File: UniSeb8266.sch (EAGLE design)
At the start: 31 parts, among them IC1 WEMOS-D1-MINI, IC2 GY-BME280-3.3, IC3 LM3940, IC4 MCP23008SS, IC5 RT9400, IC6 AMS5915, J1 22-27-2031-03, X61 JST-XH-05-PIN-LONG-PAD, X7 0446200002

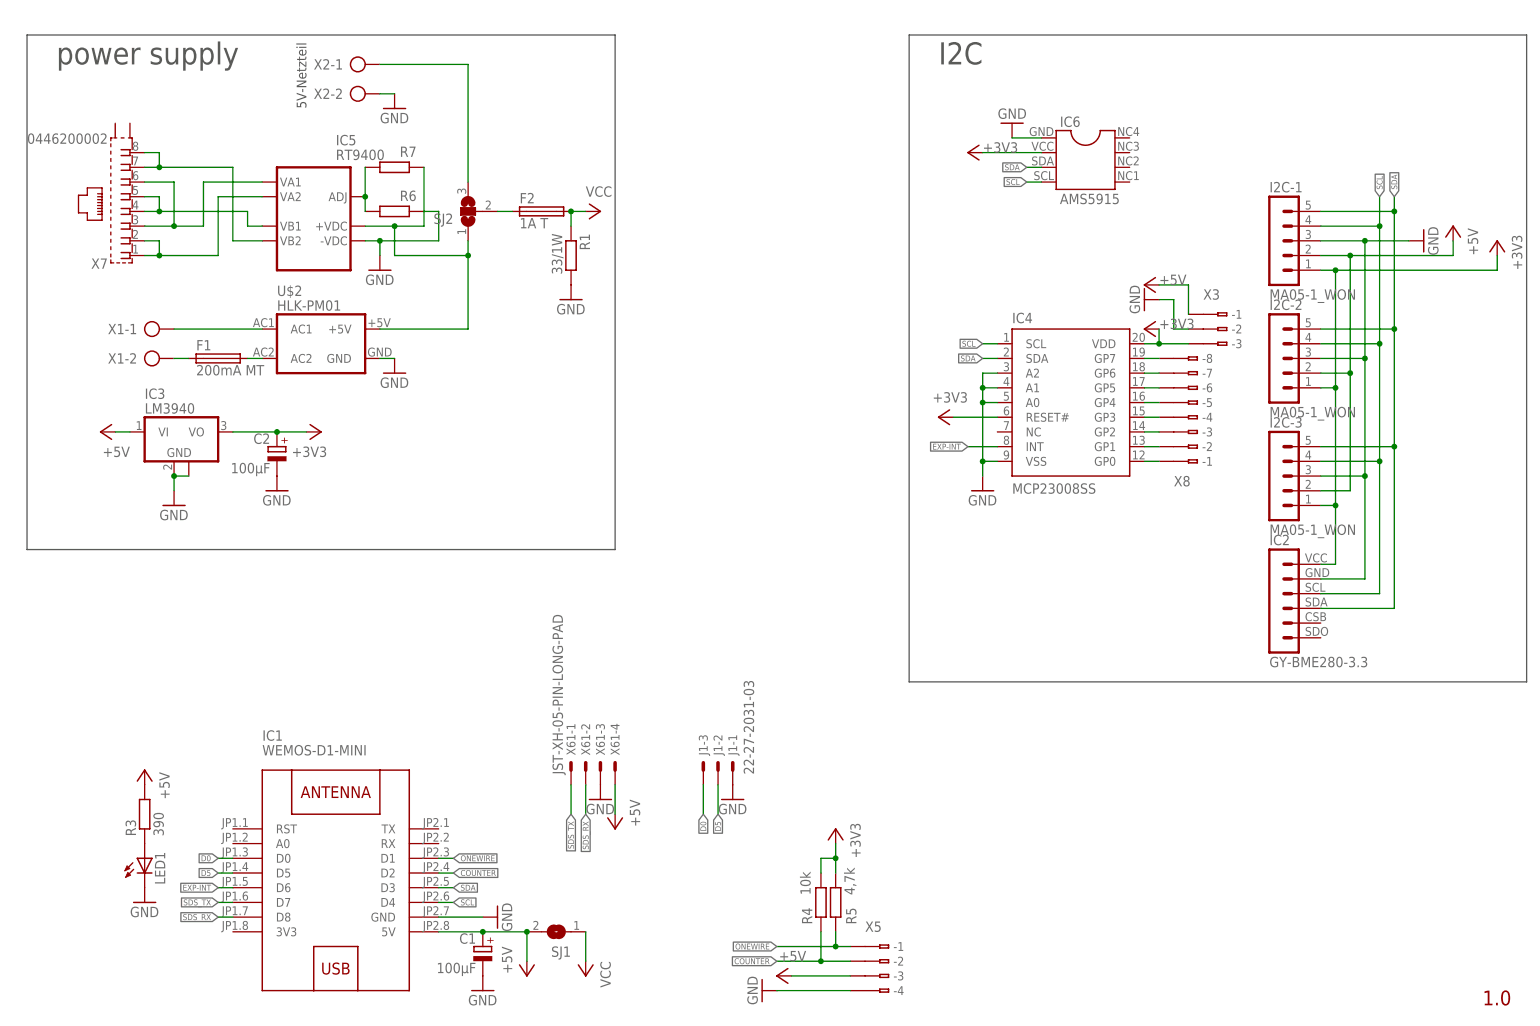
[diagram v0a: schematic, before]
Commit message: Changed the fixed voltage regulator to AMS1117/LM1117 and the output capacitor.
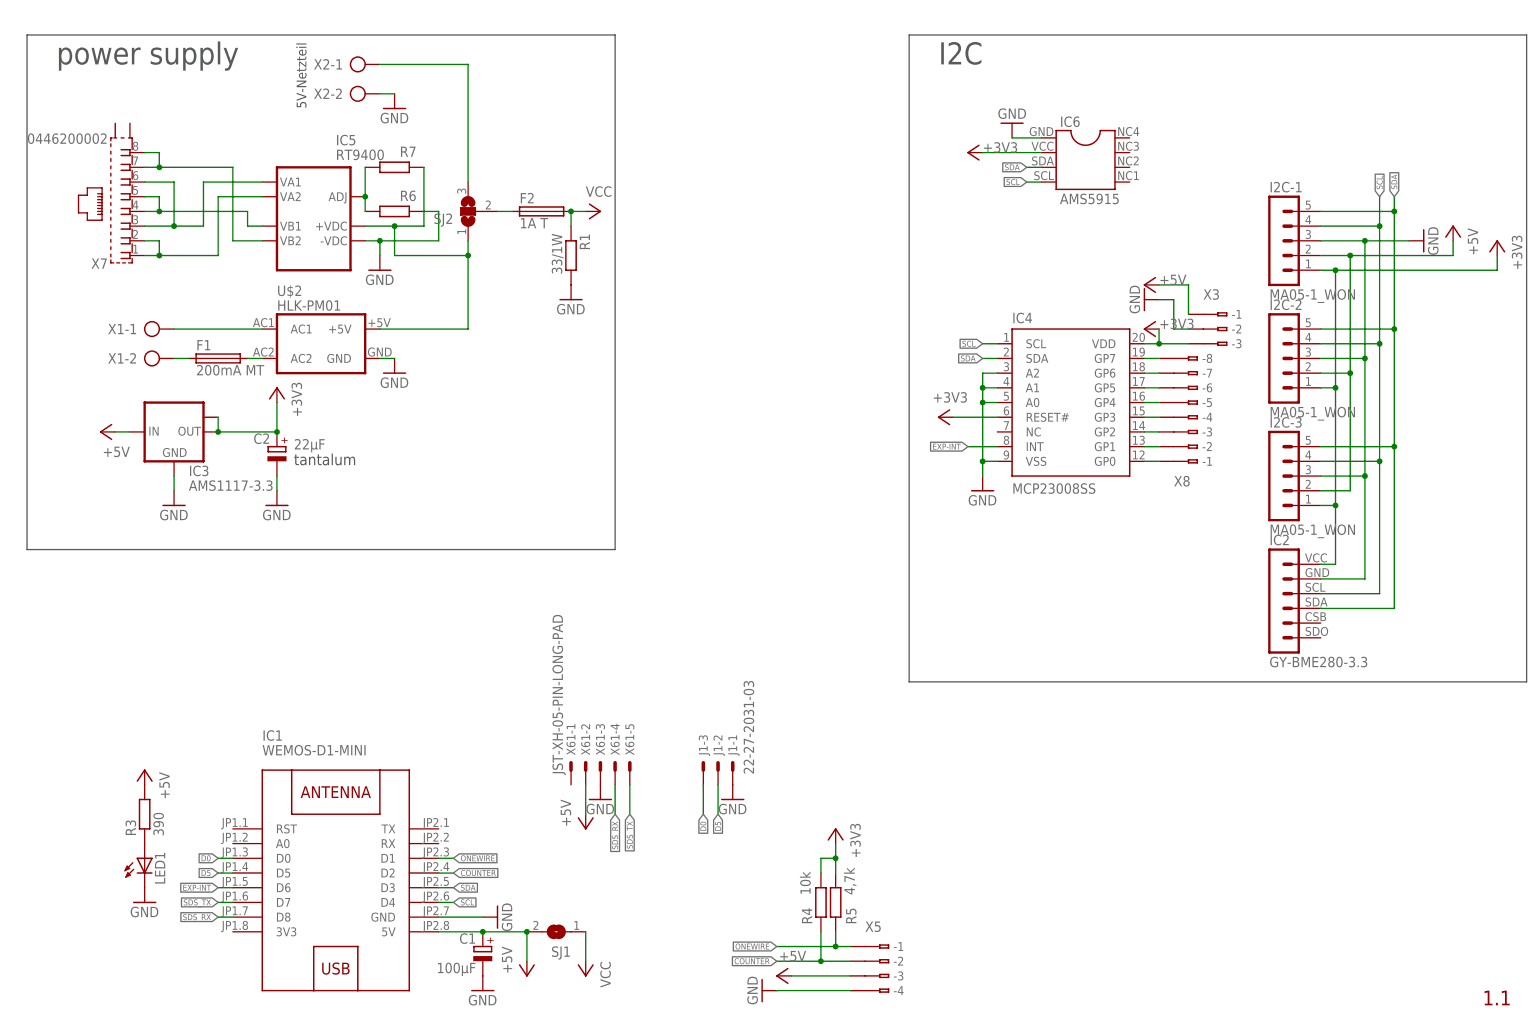
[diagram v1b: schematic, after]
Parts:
- C2: value 100µF -> 22µF
- IC3: value LM3940 -> AMS1117-3.3; device linear:UA78M33DCY -> lm1117:LM1117IMPX-3.3
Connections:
- net +3V3: now also IC3.OUT, IC3.OUT1; no longer IC3.VO
- net +5V: now also IC3.IN, X61-2.S; no longer IC3.VI, X61-4.S
- net GND: no longer IC3.GND@1
- net SDS_RX: now also X61-4.S; no longer X61-2.S
- net SDS_TX: now also X61-5.S; no longer X61-1.S
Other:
- note added: "1.1"
- note added: "tantalum"
- note removed: "1.0"
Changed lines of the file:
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@@
 <part name="GND2" library="supply1" deviceset="GND" device=""/>
 <part name="GND3" library="supply1" deviceset="GND" device=""/>
-<part name="P+3" library="supply1" deviceset="+5V" device=""/>
 <part name="SJ1" library="jumper" deviceset="SJ" device=""/>
 <part name="P+1" library="supply1" deviceset="+5V" device=""/>
@@
 <part name="P+4" library="supply1" deviceset="VCC" device=""/>
 <part name="P+8" library="supply1" deviceset="VCC" device=""/>
-<part name="IC3" library="linear" deviceset="UA78M*" device="DCY" technology="33" value="LM3940"/>
 <part name="P+2" library="supply1" deviceset="+5V" device=""/>
 <part name="GND9" library="supply1" deviceset="GND" device=""/>
@@
 <part name="C1" library="rcl" deviceset="CPOL-EU" device="E2.5-6" value="100µF"/>
 <part name="GND10" library="supply1" deviceset="GND" device=""/>
-<part name="C2" library="rcl" deviceset="CPOL-EU" device="E2.5-6" value="100µF"/>
+<part name="C2" library="rcl" deviceset="CPOL-EU" device="E2.5-6" value="22µF"/>
 <part name="GND11" library="supply1" deviceset="GND" device=""/>
 <part name="IC5" library="POE-Module" deviceset="RT9400" device=""/>
@@
 <part name="J1" library="con-molex" deviceset="22-?-03" device="27-2031"/>
 <part name="U$2" library="HLK" deviceset="HLK-PM01" device=""/>
+<part name="P+3" library="supply1" deviceset="+5V" device=""/>
+<part name="IC3" library="lm1117" deviceset="LM1117IMPX-*" device="" technology="3.3" value="AMS1117-3.3"/>
 </parts>
 <sheets>
@@
 <wire x1="261.62" y1="175.26" x2="154.94" y2="175.26" width="0.1524" layer="97"/>
 <text x="160.02" y="170.18" size="3.81" layer="97">I2C</text>
-<text x="254" y="7.62" size="2.54" layer="94">1.0</text>
+<text x="254" y="7.62" size="2.54" layer="94">1.1</text>
+<text x="48.641" y="102.87" size="1.9304" layer="97" rot="MR180">tantalum</text>
 </plain>
 <instances>
@@
 <instance part="GND2" gate="1" x="83.82" y="22.86" rot="R90"/>
 <instance part="GND3" gate="1" x="101.6" y="43.18"/>
-<instance part="P+3" gate="1" x="104.14" y="38.1" rot="R180"/>
 <instance part="SJ1" gate="1" x="93.98" y="20.32" rot="R180"/>
 <instance part="P+1" gate="1" x="88.9" y="12.7" rot="MR180"/>
@@
 <instance part="P+4" gate="VCC" x="99.06" y="12.7" rot="R180"/>
 <instance part="P+8" gate="VCC" x="101.6" y="144.78" rot="R270"/>
-<instance part="IC3" gate="G$1" x="27.94" y="106.68"/>
 <instance part="P+2" gate="1" x="15.24" y="106.68" rot="R90"/>
 <instance part="GND9" gate="1" x="27.94" y="93.98"/>
-<instance part="+3V7" gate="G$1" x="53.34" y="106.68" rot="MR90"/>
+<instance part="+3V7" gate="G$1" x="45.72" y="114.3" rot="MR0"/>
 <instance part="C1" gate="G$1" x="81.28" y="17.78" rot="MR0"/>
 <instance part="GND10" gate="1" x="81.28" y="10.16"/>
-<instance part="C2" gate="G$1" x="45.72" y="104.14" rot="MR0"/>
-<instance part="GND11" gate="1" x="45.72" y="96.52"/>
+<instance part="C2" gate="G$1" x="45.72" y="104.14" smashed="yes" rot="MR0">
+<attribute name="NAME" x="44.577" y="104.6226" size="1.778" layer="95" rot="MR0"/>
+<attribute name="VALUE" x="48.641" y="105.4354" size="1.778" layer="96" rot="MR180"/>
+</instance>
+<instance part="GND11" gate="1" x="45.72" y="93.98"/>
 <instance part="IC5" gate="G$1" x="50.8" y="137.16"/>
 <instance part="GND12" gate="1" x="63.5" y="134.62"/>
@@
 <instance part="J1" gate="-3" x="119.38" y="48.26" rot="R90"/>
 <instance part="U$2" gate="HLK-PM01" x="53.34" y="121.92"/>
+<instance part="X61" gate="-5" x="106.68" y="48.26" rot="R90"/>
+<instance part="P+3" gate="1" x="99.06" y="38.1" rot="MR180"/>
+<instance part="IC3" gate="G$1" x="27.94" y="106.68"/>
 </instances>
 <busses>
@@
 </segment>
 <segment>
-<pinref part="IC3" gate="G$1" pin="GND"/>
 <pinref part="GND9" gate="1" pin="GND"/>
 <wire x1="27.94" y1="99.06" x2="27.94" y2="96.52" width="0.1524" layer="91"/>
-<pinref part="IC3" gate="G$1" pin="GND@1"/>
-<wire x1="27.94" y1="99.06" x2="30.48" y2="99.06" width="0.1524" layer="91"/>
-<junction x="27.94" y="99.06"/>
+<pinref part="IC3" gate="G$1" pin="GND"/>
 </segment>
 <segment>
@@
 <pinref part="C2" gate="G$1" pin="-"/>
 <pinref part="GND11" gate="1" pin="GND"/>
+<wire x1="45.72" y1="96.52" x2="45.72" y2="99.06" width="0.1524" layer="91"/>
 </segment>
 <segment>
@@
 </net>
 <net name="+5V" class="0">
-<segment>
-<wire x1="104.14" y1="45.72" x2="104.14" y2="40.64" width="0.1524" layer="91"/>
-<pinref part="P+3" gate="1" pin="+5V"/>
-<pinref part="X61" gate="-4" pin="S"/>
-</segment>
 <segment>
 <pinref part="SJ1" gate="1" pin="2"/>
@@
 </segment>
 <segment>
-<pinref part="IC3" gate="G$1" pin="VI"/>
 <wire x1="20.32" y1="106.68" x2="17.78" y2="106.68" width="0.1524" layer="91"/>
 <pinref part="P+2" gate="1" pin="+5V"/>
+<pinref part="IC3" gate="G$1" pin="IN"/>
 </segment>
 <segment>
@@
 <pinref part="P+9" gate="1" pin="+5V"/>
 </segment>
+<segment>
+<pinref part="X61" gate="-2" pin="S"/>
+<pinref part="P+3" gate="1" pin="+5V"/>
+<wire x1="99.06" y1="45.72" x2="99.06" y2="40.64" width="0.1524" layer="91"/>
+</segment>
 </net>
 <net name="SDS_TX" class="0">
-<segment>
-<wire x1="96.52" y1="45.72" x2="96.52" y2="40.64" width="0.1524" layer="91"/>
-<label x="96.52" y="40.64" size="1.016" layer="95" rot="R270" xref="yes"/>
-<pinref part="X61" gate="-1" pin="S"/>
-</segment>
 <segment>
 <pinref part="IC1" gate="G$1" pin="D7"/>
 <wire x1="38.1" y1="25.4" x2="35.56" y2="25.4" width="0.1524" layer="91"/>
 <label x="35.56" y="25.4" size="1.016" layer="95" rot="R180" xref="yes"/>
+</segment>
+<segment>
+<wire x1="106.68" y1="45.72" x2="106.68" y2="40.64" width="0.1524" layer="91"/>
+<label x="106.68" y="40.64" size="1.016" layer="95" rot="R270" xref="yes"/>
+<pinref part="X61" gate="-5" pin="S"/>
 </segment>
 </net>
@@
 </segment>
 <segment>
-<pinref part="IC3" gate="G$1" pin="VO"/>
 <pinref part="+3V7" gate="G$1" pin="+3V3"/>
-<wire x1="38.1" y1="106.68" x2="45.72" y2="106.68" width="0.1524" layer="91"/>
+<wire x1="35.56" y1="106.68" x2="45.72" y2="106.68" width="0.1524" layer="91"/>
 <pinref part="C2" gate="G$1" pin="+"/>
-<wire x1="45.72" y1="106.68" x2="50.8" y2="106.68" width="0.1524" layer="91"/>
+<wire x1="45.72" y1="106.68" x2="45.72" y2="111.76" width="0.1524" layer="91"/>
 <junction x="45.72" y="106.68"/>
+<pinref part="IC3" gate="G$1" pin="OUT"/>
+<pinref part="IC3" gate="G$1" pin="OUT1"/>
+<wire x1="35.56" y1="109.22" x2="35.56" y2="106.68" width="0.1524" layer="91"/>
+<junction x="35.56" y="106.68"/>
 </segment>
 <segment>
@@
 <net name="SDS_RX" class="0">
 <segment>
-<wire x1="99.06" y1="45.72" x2="99.06" y2="40.64" width="0.1524" layer="91"/>
-<label x="99.06" y="40.64" size="1.016" layer="95" rot="R270" xref="yes"/>
-<pinref part="X61" gate="-2" pin="S"/>
-</segment>
-<segment>
 <pinref part="IC1" gate="G$1" pin="D8"/>
 <wire x1="38.1" y1="22.86" x2="35.56" y2="22.86" width="0.1524" layer="91"/>
 <label x="35.56" y="22.86" size="1.016" layer="95" rot="R180" xref="yes"/>
 </segment>
-</net>
+<segment>
+<wire x1="104.14" y1="45.72" x2="104.14" y2="40.64" width="0.1524" layer="91"/>
+<label x="104.14" y="40.64" size="1.016" layer="95" rot="R270" xref="yes"/>
+<pinref part="X61" gate="-4" pin="S"/>
+</segment>
+</net>
